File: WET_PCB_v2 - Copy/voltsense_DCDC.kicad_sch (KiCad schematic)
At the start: 9 parts, among them J17 Capacitor connector, U1 Opamp_Quad

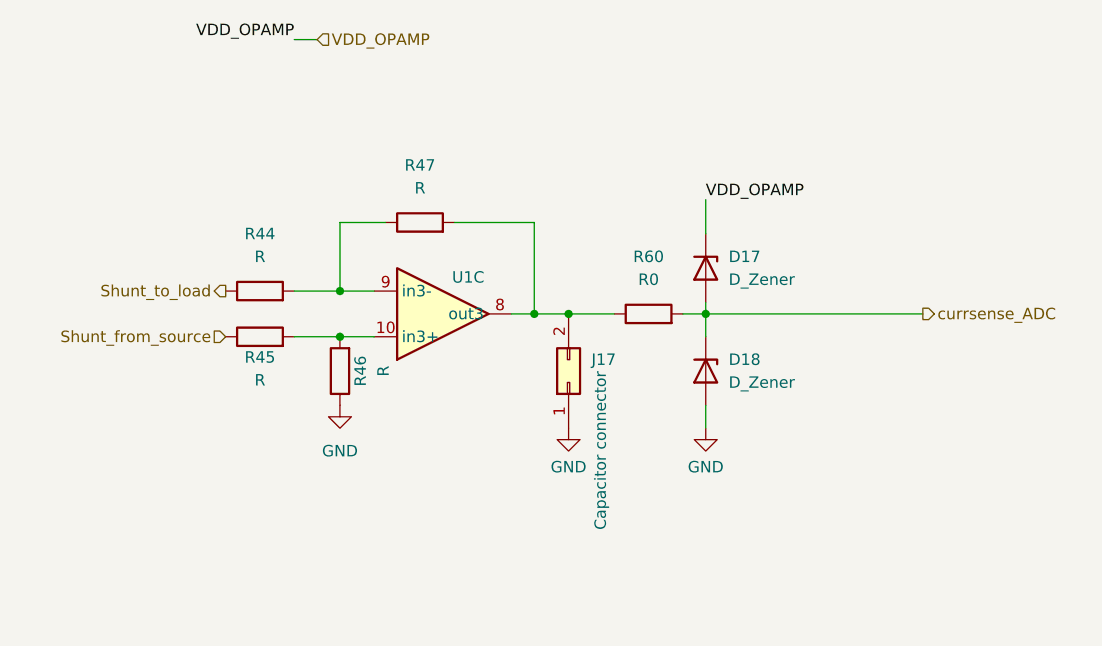
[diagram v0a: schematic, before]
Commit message: microcontroller to chip traces done
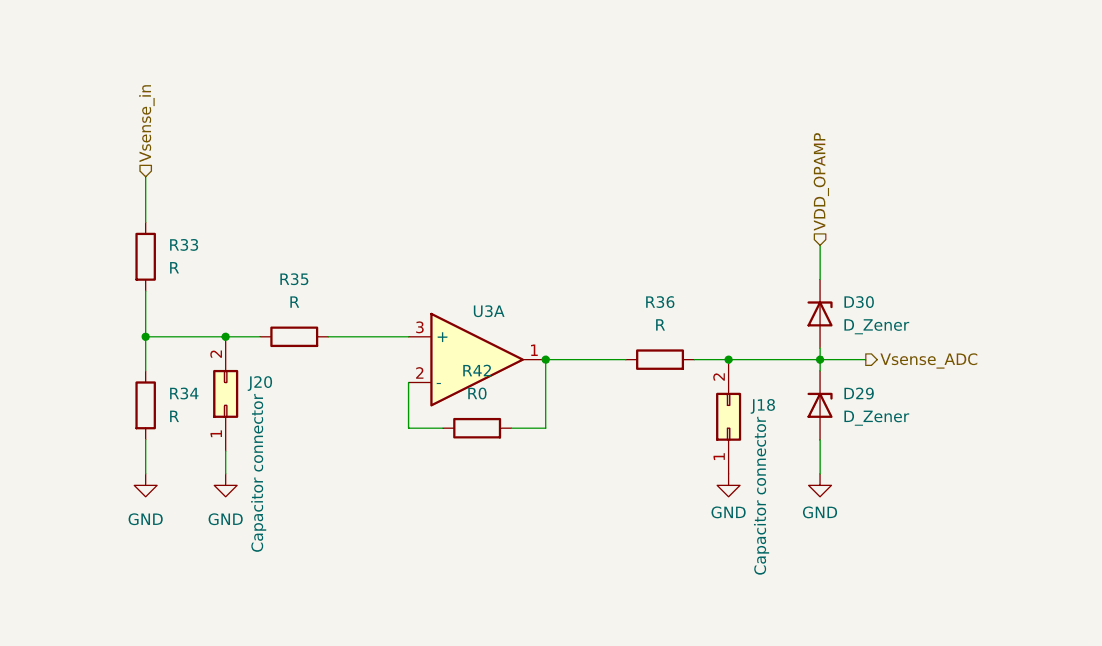
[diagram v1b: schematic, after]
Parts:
- removed D17, D18: D_Zener, Diode_SMD:D_SMF, symbol Device:D_Zener
- removed J17: Capacitor connector, Connector_PinSocket_2.54mm:PinSocket_1x02_P2.54mm_Horizontal, symbol Connector_Generic:Conn_02x01
- removed R44, R45, R46, R47: R, Resistor_SMD:R_0805_2012Metric_Pad1.20x1.40mm_HandSolder, symbol Device:R
- removed R60: R0, Resistor_SMD:R_0805_2012Metric_Pad1.20x1.40mm_HandSolder, symbol Device:R
- removed U1: Opamp_Quad, Package_DIP:DIP-14_W7.62mm, symbol Device:Opamp_Quad
- added D29, D30: D_Zener, Diode_THT:D_DO-15_P2.54mm_Vertical_CathodeUp, symbol Device:D_Zener
- added J18, J20: Capacitor connector, Connector_PinSocket_2.54mm:PinSocket_1x02_P2.54mm_Vertical, symbol Connector_Generic:Conn_02x01
- added R33, R34, R35, R36: R, Resistor_SMD:R_0805_2012Metric_Pad1.20x1.40mm_HandSolder, symbol Device:R
- added R42: R0, Resistor_SMD:R_0805_2012Metric_Pad1.20x1.40mm_HandSolder, symbol Device:R
- added U3: Opamp_Quad, symbol Device:Opamp_Quad
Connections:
- net GND: now also D29.2 (A), J18.1 (Pin_1), J20.1 (Pin_1), R34.2
- net VDD_OPAMP: now also D30.1 (K)
- new net: J20.2 (Pin_2), R33.2, R34.1, R35.1
- new net: R35.2, U3.3 (+)
- new net: R36.1, R42.2, U3.1
- new net: R42.1, U3.2 (-)
- new net Vsense_ADC: D29.1 (K), D30.2 (A), J18.2 (Pin_2), R36.2
- new net Vsense_in: R33.1
